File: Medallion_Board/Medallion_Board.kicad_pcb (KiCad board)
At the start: 2 copper layers, 42 parts, among them Q3 DMG3415U, SW1 KMR2, SW2 KMR2, U2 AP2112/RT9080-3.3, U3 ESP32-S3-MINI-1-N8, U4 LC709203FQH-01TWG, U5 MCP73831T-2ACI_OT, X1 JSTPH, X2 USB4085-GF-A

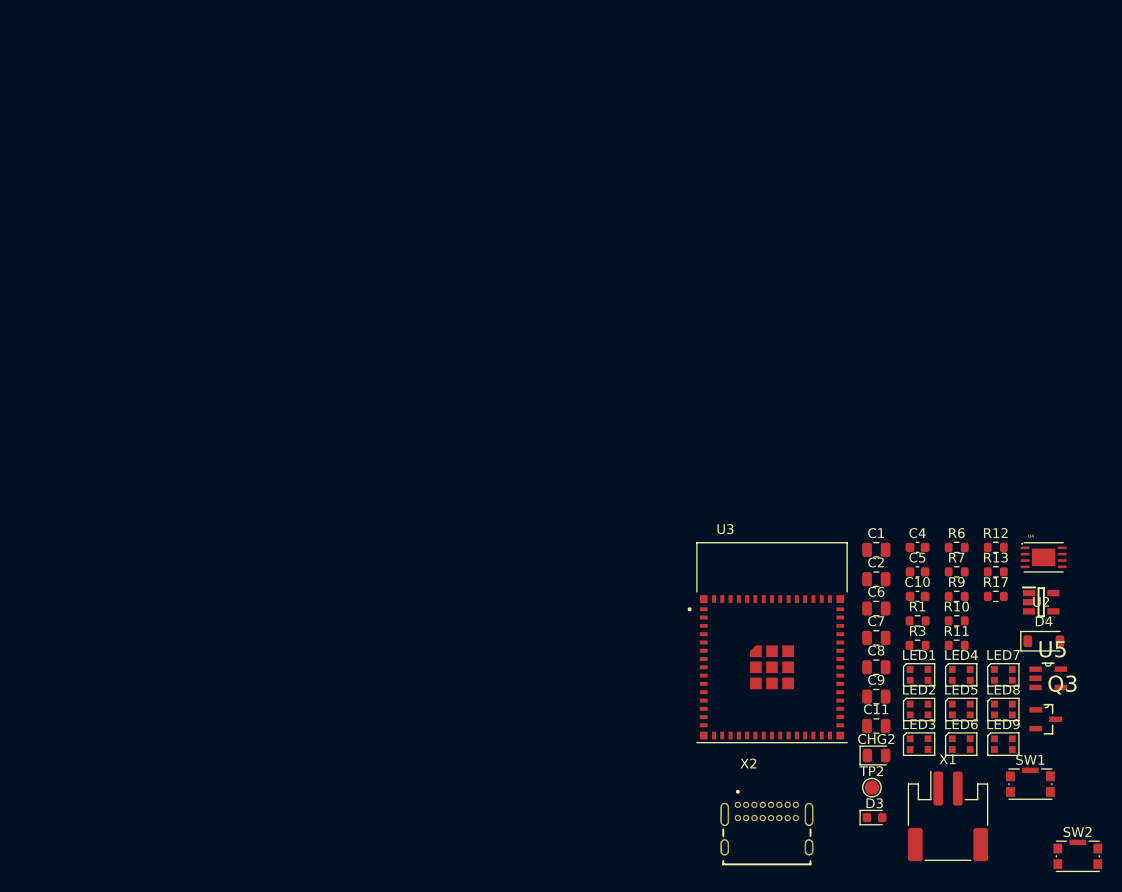
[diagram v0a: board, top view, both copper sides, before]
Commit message: More fiddling. Added 3D models to the components
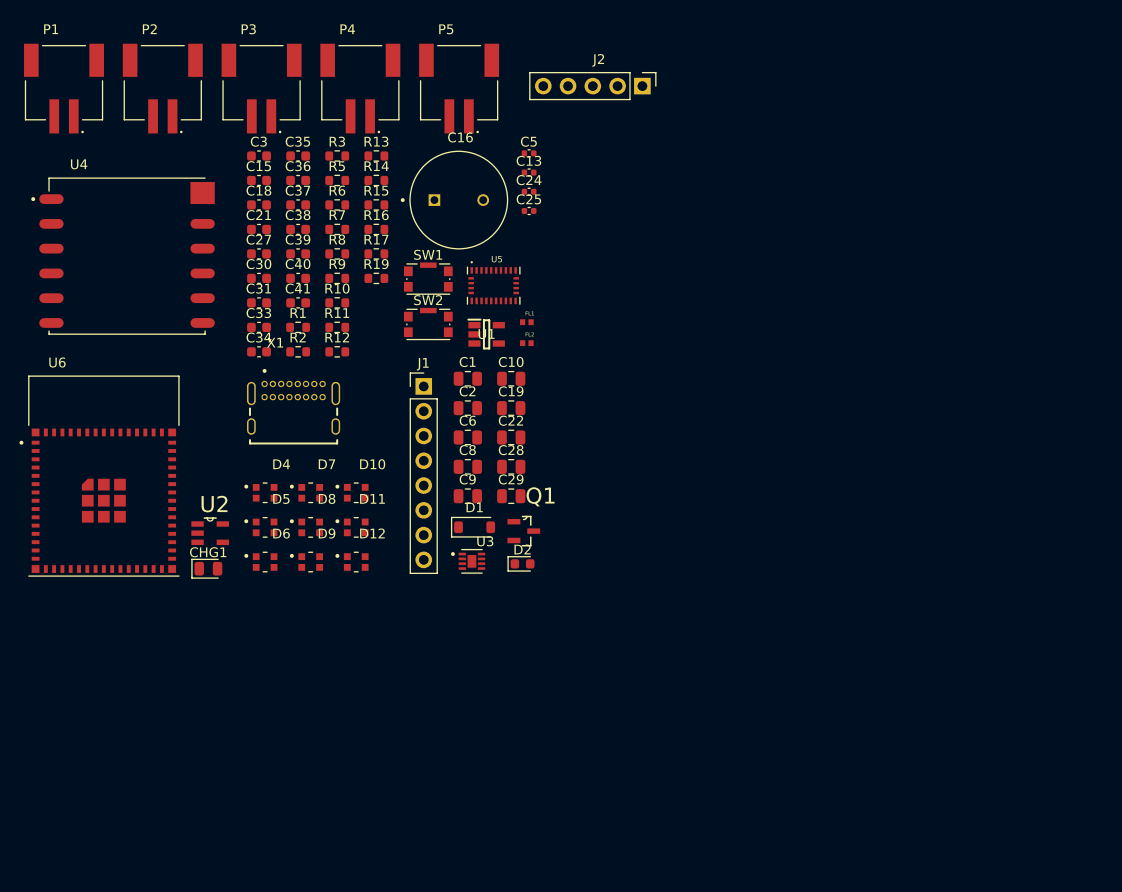
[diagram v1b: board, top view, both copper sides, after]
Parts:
- removed C11: 10µF, Capacitor_SMD:C_0805_2012Metric
- removed C4: 1uF, Capacitor_SMD:C_0603_1608Metric
- removed C7: 10uF, Capacitor_SMD:C_0805_2012Metric
- removed CHG2: ORANGE, LED_SMD:LED_0805_2012Metric
- removed D3: RED, LED_SMD:LED_0603_1608Metric
- removed LED1, LED2, LED3, LED4, LED5, LED6, LED7, LED8, LED9: WS2812B_SK6805_1515, LED_SMD:LED_WS2812B-2020_PLCC4_2.0x2.0mm
- removed Q3: DMG3415U, DMG3415U-7:SOT95P240X105-3N
- removed TP2: TESTPOINTROUND1.5MMNO, TestPoint:TestPoint_Pad_D1.5mm
- removed X2: USB4085-GF-A, USB4085-GF-A:GCT_USB4085-GF-A_REVB
- added C13: 0.1uF, Capacitor_SMD:C_0402_1005Metric, F.Cu at (71.2, 33.3)
- added C15: 100nF, Capacitor_SMD:C_0603_1608Metric, F.Cu at (43.6, 34.1)
- added C16: KW-5R5C104-R, KW-5R5C104-R:CAPPRD500W60D1000H3150, F.Cu at (64.0, 36.1)
- added C18: 100nF, Capacitor_SMD:C_0603_1608Metric, F.Cu at (43.6, 36.6)
- added C19: 10uF, Capacitor_SMD:C_0805_2012Metric, F.Cu at (69.4, 57.5)
- added C21: 100nF, Capacitor_SMD:C_0603_1608Metric, F.Cu at (43.6, 39.2)
- added C22: 10uF, Capacitor_SMD:C_0805_2012Metric, F.Cu at (69.4, 60.5)
- added C24: 0.1uF, Capacitor_SMD:C_0402_1005Metric, F.Cu at (71.2, 35.3)
- added C25: 47pF, Capacitor_SMD:C_0402_1005Metric, F.Cu at (71.2, 37.3)
- added C27: 100nF, Capacitor_SMD:C_0603_1608Metric, F.Cu at (43.6, 41.7)
- added C28: 10uF, Capacitor_SMD:C_0805_2012Metric, F.Cu at (69.4, 63.5)
- added C29: 10uF, Capacitor_SMD:C_0805_2012Metric, F.Cu at (69.4, 66.5)
- added C3: 1uF, Capacitor_SMD:C_0603_1608Metric, F.Cu at (43.6, 31.6)
- added C30: 1uF, Capacitor_SMD:C_0603_1608Metric, F.Cu at (43.6, 44.2)
- added C31: 1uF, Capacitor_SMD:C_0603_1608Metric, F.Cu at (43.6, 46.7)
- added C33: 0.1µF, Capacitor_SMD:C_0603_1608Metric, F.Cu at (43.6, 49.2)
- added C34: 0.1µF, Capacitor_SMD:C_0603_1608Metric, F.Cu at (43.6, 51.7)
- added C35: 0.1µF, Capacitor_SMD:C_0603_1608Metric, F.Cu at (47.6, 31.6)
- added C36: 0.1µF, Capacitor_SMD:C_0603_1608Metric, F.Cu at (47.6, 34.1)
- added C37: 0.1µF, Capacitor_SMD:C_0603_1608Metric, F.Cu at (47.6, 36.6)
- added C38: 0.1µF, Capacitor_SMD:C_0603_1608Metric, F.Cu at (47.6, 39.2)
- added C39: 0.1µF, Capacitor_SMD:C_0603_1608Metric, F.Cu at (47.6, 41.7)
- added C40: 0.1µF, Capacitor_SMD:C_0603_1608Metric, F.Cu at (47.6, 44.2)
- added C41: 0.1µF, Capacitor_SMD:C_0603_1608Metric, F.Cu at (47.6, 46.7)
- added CHG1: ORANGE, LED_SMD:LED_0805_2012Metric, F.Cu at (38.4, 73.9)
- added D1: MBR0540, Diode_SMD:D_SOD-123, F.Cu at (65.7, 69.7)
- added D10: WS2812B2020, WS2812B2020:LED_WS2812B2020, F.Cu at (53.5, 66.2)
- added D11: WS2812B2020, WS2812B2020:LED_WS2812B2020, F.Cu at (53.5, 69.7)
- added D12: WS2812B2020, WS2812B2020:LED_WS2812B2020, F.Cu at (53.5, 73.3)
- added D2: RED, LED_SMD:LED_0603_1608Metric, F.Cu at (70.6, 73.4)
- added D5: WS2812B2020, WS2812B2020:LED_WS2812B2020, F.Cu at (44.2, 69.7)
- added D6: WS2812B2020, WS2812B2020:LED_WS2812B2020, F.Cu at (44.2, 73.3)
- added D7: WS2812B2020, WS2812B2020:LED_WS2812B2020, F.Cu at (48.9, 66.2)
- added D8: WS2812B2020, WS2812B2020:LED_WS2812B2020, F.Cu at (48.9, 69.7)
- added D9: WS2812B2020, WS2812B2020:LED_WS2812B2020, F.Cu at (48.9, 73.3)
- added FL1: BLM15EG121SN1D, BLM15EG121SN1D:BEADC1005X55N, F.Cu at (71.0, 48.7)
- added FL2: BLM15EG121SN1D, BLM15EG121SN1D:BEADC1005X55N, F.Cu at (71.0, 50.8)
- added J1: EXPANSION, Connector_PinHeader_2.54mm:PinHeader_1x08_P2.54mm_Vertical, F.Cu at (60.4, 55.3)
- added J2: RYLR998, Connector_PinHeader_2.54mm:RYLR998, F.Cu at (77.9, 24.2)
- added P1: JST_EN, S2B-PH-SM4-TB_LF__SN_:JST_S2B-PH-SM4-TB_LF__SN_, F.Cu at (23.6, 27.6)
- added P2: JST_PH, S2B-PH-SM4-TB_LF__SN_:JST_S2B-PH-SM4-TB_LF__SN_, F.Cu at (33.7, 27.6)
- added P3: JST_BTN_1, S2B-PH-SM4-TB_LF__SN_:JST_S2B-PH-SM4-TB_LF__SN_, F.Cu at (43.8, 27.6)
- added P4: JST_BTN_2, S2B-PH-SM4-TB_LF__SN_:JST_S2B-PH-SM4-TB_LF__SN_, F.Cu at (53.9, 27.6)
- added P5: JST_BTN_3, S2B-PH-SM4-TB_LF__SN_:JST_S2B-PH-SM4-TB_LF__SN_, F.Cu at (64.1, 27.6)
- added Q1: DMG3415U, DMG3415U-7:SOT95P240X105-3N, F.Cu at (70.7, 70.1)
- added R14: 10K, Resistor_SMD:R_0603_1608Metric, F.Cu at (55.6, 34.1)
- added R15: 10K, Resistor_SMD:R_0603_1608Metric, F.Cu at (55.6, 36.6)
- added R16: 5.1K, Resistor_SMD:R_0603_1608Metric, F.Cu at (55.6, 39.2)
- added R19: 0.5K, Resistor_SMD:R_0603_1608Metric, F.Cu at (55.6, 44.2)
- added R2: 5.1K, Resistor_SMD:R_0603_1608Metric, F.Cu at (47.6, 51.7)
- added R5: 100K, Resistor_SMD:R_0603_1608Metric, F.Cu at (51.6, 34.1)
- added R8: 5.1K, Resistor_SMD:R_0603_1608Metric, F.Cu at (51.6, 41.7)
- added U1: RT9080-33GJ5, RT9080-33GJ5:SOT94P280X100-5N, F.Cu at (66.9, 49.9)
- added U6: ESP32-S3-MINI-1-N8, ESP32-S3-MINI-1-N8:XCVR_ESP32-S3-MINI-1-N8, F.Cu at (27.6, 67.0)
- C1: value 10uF -> 22µF
- C10: value 1uF -> 10uF; footprint Capacitor_SMD:C_0603_1608Metric -> Capacitor_SMD:C_0805_2012Metric
- C2: value 10uF -> 10µF
- C5: value 1uF -> 0.1µF; footprint Capacitor_SMD:C_0603_1608Metric -> Capacitor_SMD:C_0402_1005Metric
- D4: value MBR540 -> WS2812B2020; footprint Diode_SMD:D_SOD-123 -> WS2812B2020:LED_WS2812B2020
- R1: value 5.1K -> 100K
- R10, R11, R13, R9: value 5.1K -> 10K
- R12: value 100K -> 1K
- R3: value 10K -> 2K
- R7: value 100K -> 5.1K
- U2: value AP2112/RT9080-3.3 -> MCP73831T-2ACI_OT; footprint RT9080-33GJ5:SOT94P280X100-5N -> MCP73831T-2ACI_OT:SOT95P280X145-5N
- U3: value ESP32-S3-MINI-1-N8 -> MAX17048G_T10; footprint ESP32-S3-MINI-1-N8:XCVR_ESP32-S3-MINI-1-N8 -> MAX17048G_T10:SON50P200X200X80-9N
- U4: value LC709203FQH-01TWG -> LC86LICMD; footprint LC709203FQH-01TWG:DFN300X400X80-8N -> LC86LICMD:MODULE_LC86LICMD
- U5: value MCP73831T-2ACI_OT -> BNO085; footprint MCP73831T-2ACI_OT:SOT95P280X145-5N -> BNO085:IC_BNO085
- X1: value JSTPH -> USB4085-GF-A; footprint Connector_JST:JST_PH_S2B-PH-SM4-TB_1x02-1MP_P2.00mm_Horizontal -> USB4085-GF-A:GCT_USB4085-GF-A_REVB
- moved U4 98.9 mm to (30.0, 41.9)
- moved SW2 86.1 mm to (60.9, 48.9)
- moved U2 85.5 mm to (38.6, 70.3)
- moved D4 81.3 mm to (44.2, 66.2)
- moved SW1 80.6 mm to (60.9, 44.2)
- moved X1 78.1 mm to (47.1, 59.4)
- moved R3 77.8 mm to (51.6, 31.6)
- moved R13 76.5 mm to (55.6, 31.6)
- moved R17 72.6 mm to (55.6, 41.7)
- moved R7 72.6 mm to (51.6, 39.2)
- moved R6 72.6 mm to (51.6, 36.6)
- moved R11 71.4 mm to (51.6, 49.2)
- moved R9 71.4 mm to (51.6, 44.2)
- moved R10 71.4 mm to (51.6, 46.7)
- moved R12 70.4 mm to (51.6, 51.7)
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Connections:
- C1 pad 1: 3.3V -> VBAT
- C2 pad 1: 3.3V -> /VHI
- C5 pad 1: /IO34_DBLTAP -> Net-(U1-P4)
- C6 pad 1: /VHI -> 3.3V
- C8 pad 1: 3.3V -> VBAT
- D4 pad 1: VBUS -> Net-(D4-DO)
- D4 pad 2: /VHI -> GND
- R1 pad 1: /RESET -> GND
- R1 pad 2: 3.3V -> VBUS
- R10 pad 1: /D13 -> /SDA
- R10 pad 2: Net-(D3-Pad2) -> +3.3V
- R11 pad 1: GND -> /USER_BTN_1
- R11 pad 2: Net-(X2-CC1) -> +3.3V
- R12 pad 1: GND -> 3.3V
- R12 pad 2: VBUS -> Net-(U4-V_BCKP)
- R13 pad 1: GND -> /USER_BTN_2
- R13 pad 2: Net-(X2-CC2) -> +3.3V
- R3 pad 1: /SCL -> GND
- R3 pad 2: /SDA -> Net-(U2-PROG)
- R6 pad 2: Net-(U5-STAT) -> Net-(U2-STAT)
- R7 pad 1: /EN -> GND
- R7 pad 2: /VHI -> Net-(X1-CC1)
- R9 pad 1: GND -> /SCL
- R9 pad 2: Net-(U5-PROG) -> +3.3V
- SW1 pad 2: /BOOT0 -> /RESET
- SW2 pad 2: /RESET -> /BOOT0
- U2 pad 1: /VHI -> Net-(U2-STAT)
- U2 pad 3: /EN -> VBAT
- U2 pad 4: unconnected-(U2-P4-Pad4) -> VBUS
- U2 pad 5: 3.3V -> Net-(U2-PROG)
- U3 pad 2: GND -> VBAT
- U3 pad 3: 3.3V -> VBAT
- U3 pad 4: /BOOT0 -> GND
- U3 pad 5: unconnected-(U3-IO1-Pad5) -> /LOW_BATT
- U3 pad 6: unconnected-(U3-IO2-Pad6) -> GND
- U3 pad 7: /SDA -> /SCL
- U3 pad 8: /SCL -> /SDA
- U3 pad 9: unconnected-(U3-IO5-Pad9) -> GND
- U4 pad 1: GND -> /TXD0
- U4 pad 2: GND -> /RXD0
- U4 pad 3: VBAT -> GND
- U4 pad 4: unconnected-(U4-ALARMB-Pad4) -> 3.3V
- U4 pad 5: unconnected-(U4-TSW-Pad5) -> Net-(U4-V_BCKP)
- U4 pad 7: /SDA -> /GPS_WAKEUP
- U4 pad 8: /SCL -> /GPS_ANT_ACTIVE
- U5 pad 1: Net-(U5-STAT) -> unconnected-(U5-RESV_NC-Pad1)
- U5 pad 3: VBAT -> 3.3V
- U5 pad 4: VBUS -> Net-(U5-~{BOOT})
- U5 pad 5: Net-(U5-PROG) -> GND

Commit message: Categorise pcb layout by specsheet boxes
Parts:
- removed C33, C34, C35, C36, C37, C38, C39, C40, C41: 0.1µF, Capacitor_SMD:C_0603_1608Metric
- removed D12: WS2812B2020, WS2812B2020:LED_WS2812B2020
- removed R19: 0.5K, Resistor_SMD:R_0603_1608Metric
- added C11: 10uF, Capacitor_SMD:C_0805_2012Metric, F.Cu at (86.2, 78.0)
- added C12: 0.1µF, Capacitor_SMD:C_0402_1005Metric, F.Cu at (96.7, 88.0)
- added C14: 1uF, Capacitor_SMD:C_0603_1608Metric, F.Cu at (238.5, 145.5)
- added C17: 100nF, Capacitor_SMD:C_0603_1608Metric, F.Cu at (202.4, 86.4)
- added C20: 100nF, Capacitor_SMD:C_0603_1608Metric, F.Cu at (119.2, 175.0)
- added C23: 0.1µF, Capacitor_SMD:C_0603_1608Metric, F.Cu at (26.5, 25.9)
- added C26: 0.1µF, Capacitor_SMD:C_0603_1608Metric, F.Cu at (41.0, 32.8)
- added C4: KW-5R5C104-R, KW-5R5C104-R:CAPPRD500W60D1000H3150, F.Cu at (150.5, 28.5)
- added C7: 0.1uF, Capacitor_SMD:C_0402_1005Metric, F.Cu at (45.0, 143.5)
- added D3: WS2812B2020, WS2812B2020:LED_WS2812B2020, F.Cu at (25.4, 32.5)
- added R4: 1Meg, Resistor_SMD:R_0603_1608Metric, F.Cu at (246.5, 145.5)
- C1: value 22µF -> 10uF
- C10, C9: value 10uF -> 10µF
- C13: value 0.1uF -> 10uF; footprint Capacitor_SMD:C_0402_1005Metric -> Capacitor_SMD:C_0805_2012Metric
- C16: value KW-5R5C104-R -> 100nF; footprint KW-5R5C104-R:CAPPRD500W60D1000H3150 -> Capacitor_SMD:C_0603_1608Metric
- C18: value 100nF -> 1uF
- C19: value 10uF -> 0.1uF; footprint Capacitor_SMD:C_0805_2012Metric -> Capacitor_SMD:C_0402_1005Metric
- C2, C6: value 10µF -> 10uF
- C21: value 100nF -> 10µF; footprint Capacitor_SMD:C_0603_1608Metric -> Capacitor_SMD:C_0805_2012Metric
- C22, C28, C29: value 10uF -> 0.1µF; footprint Capacitor_SMD:C_0805_2012Metric -> Capacitor_SMD:C_0603_1608Metric
- C24: value 0.1uF -> 0.1µF; footprint Capacitor_SMD:C_0402_1005Metric -> Capacitor_SMD:C_0603_1608Metric
- C25: value 47pF -> 0.1µF; footprint Capacitor_SMD:C_0402_1005Metric -> Capacitor_SMD:C_0603_1608Metric
- C27: value 100nF -> 0.1µF
- C30: value 1uF -> 0.1µF
- C31: value 1uF -> 22µF; footprint Capacitor_SMD:C_0603_1608Metric -> Capacitor_SMD:C_0805_2012Metric
- C5: value 0.1µF -> 10uF; footprint Capacitor_SMD:C_0402_1005Metric -> Capacitor_SMD:C_0805_2012Metric
- C8: value 10µF -> 47pF; footprint Capacitor_SMD:C_0805_2012Metric -> Capacitor_SMD:C_0402_1005Metric
- J1: value EXPANSION -> RYLR998; footprint Connector_PinHeader_2.54mm:PinHeader_1x08_P2.54mm_Vertical -> Connector_PinHeader_2.54mm:RYLR998
- J2: value RYLR998 -> EXPANSION; footprint Connector_PinHeader_2.54mm:RYLR998 -> Connector_PinHeader_2.54mm:PinHeader_1x08_P2.54mm_Vertical
- P1: value JST_EN -> JST_PH
- P2: value JST_PH -> JST_BTN_1
- P3: value JST_BTN_1 -> JST_BTN_2
- P4: value JST_BTN_2 -> JST_BTN_3
- P5: value JST_BTN_3 -> JST_EN
- R1: value 100K -> 1K
- R12: value 1K -> 10K
- R14: value 10K -> 5.1K
- R15: value 10K -> 2K
- R17: value 1Meg -> 0.5K
- R2: value 5.1K -> 100K
- R3: value 2K -> 100K
- R5: value 100K -> 5.1K
- R8: value 5.1K -> 10K
- U2: value MCP73831T-2ACI_OT -> LC86LICMD; footprint MCP73831T-2ACI_OT:SOT95P280X145-5N -> LC86LICMD:MODULE_LC86LICMD
- U3: value MAX17048G_T10 -> ESP32-S3-MINI-1-N8; footprint MAX17048G_T10:SON50P200X200X80-9N -> ESP32-S3-MINI-1-N8:XCVR_ESP32-S3-MINI-1-N8
- U4: value LC86LICMD -> BNO085; footprint LC86LICMD:MODULE_LC86LICMD -> BNO085:IC_BNO085
- U5: value BNO085 -> MAX17048G_T10; footprint BNO085:IC_BNO085 -> MAX17048G_T10:SON50P200X200X80-9N
- U6: value ESP32-S3-MINI-1-N8 -> MCP73831T-2ACI_OT; footprint ESP32-S3-MINI-1-N8:XCVR_ESP32-S3-MINI-1-N8 -> MCP73831T-2ACI_OT:SOT95P280X145-5N
- moved C3 224.5 mm to (238.5, 143.0)
- moved X1 215.9 mm to (263.0, 54.5)
- moved C18 210.7 mm to (254.0, 48.1)
- moved R5 210.5 mm to (262.0, 40.6)
- moved R6 210.5 mm to (262.0, 43.1)
- moved R7 210.5 mm to (262.0, 45.6)
- moved SW1 208.1 mm to (268.9, 38.6)
- moved SW2 208.1 mm to (268.9, 43.3)
- moved C1 198.4 mm to (242.5, 143.0)
- moved C2 198.4 mm to (242.5, 146.0)
- moved R11 195.2 mm to (227.3, 134.1)
- moved U3 192.8 mm to (249.0, 132.0)
- moved R12 192.1 mm to (227.7, 128.5)
- moved P5 189.7 mm to (253.2, 43.2)
- moved J2 168.3 mm to (214.0, 123.3), turned to 0 degrees
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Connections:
- C1 pad 1: VBAT -> 3.3V
- C13 pad 1: GND -> 3.3V
- C13 pad 2: VBAT -> GND
- C16 pad 1: Net-(U4-V_BCKP) -> GND
- C16 pad 2: GND -> /USER_BTN_2
- C18 pad 1: GND -> /RESET
- C18 pad 2: /USER_BTN_2 -> GND
- C19 pad 1: +3.3V -> GND
- C19 pad 2: GND -> VBAT
- C2 pad 1: /VHI -> 3.3V
- C21 pad 1: GND -> VBAT
- C21 pad 2: /USER_BTN_3 -> GND
- C22 pad 1: Net-(J2-VDD) -> VBAT
- C24 pad 1: Net-(J2-VDD) -> VBAT
- C25 pad 1: Net-(J2-VDD) -> VBAT
- C27 pad 1: Net-(U5-CAP) -> VBAT
- C28 pad 1: 3.3V -> VBAT
- C29 pad 1: 3.3V -> VBAT
- C3 pad 1: /RESET -> 3.3V
- C30 pad 1: 3.3V -> VBAT
- C31 pad 1: /IO34_DBLTAP -> VBAT
- C5 pad 1: Net-(U1-P4) -> +3.3V
- C6 pad 1: 3.3V -> Net-(J1-VDD)
- C8 pad 1: VBAT -> Net-(J1-VDD)
- C9 pad 1: 3.3V -> /VHI
- D11 pad 1: Net-(D11-DO) -> unconnected-(D11-DO-Pad1)
- FL1 pad 2: Net-(J2-VDD) -> Net-(J1-VDD)
- J1 pad 1: /GPIO01 -> Net-(J1-VDD)
- J1 pad 2: /GPIO02 -> /LORA_NRST
- J1 pad 3: /GPIO06 -> /TXD1
- J1 pad 4: /GPIO11 -> /RXD1
- J1 pad 5: /SDA -> GND
- J2 pad 1: Net-(J2-VDD) -> /GPIO01
- J2 pad 2: /LORA_NRST -> /GPIO02
- J2 pad 3: /TXD1 -> /GPIO06
- J2 pad 4: /RXD1 -> /GPIO11
- J2 pad 5: GND -> /SDA
- P1 pad 1: /RESET -> VBAT
- P2 pad 1: VBAT -> /USER_BTN_1
- P3 pad 1: /USER_BTN_1 -> /USER_BTN_2
- P4 pad 1: /USER_BTN_2 -> /USER_BTN_3
- P5 pad 1: /USER_BTN_3 -> /RESET
- R1 pad 1: GND -> 3.3V
- R1 pad 2: VBUS -> Net-(U2-V_BCKP)
- R10 pad 1: /SDA -> /USER_BTN_3
- R11 pad 1: /USER_BTN_1 -> /SCL
- R12 pad 1: 3.3V -> /SDA
- R12 pad 2: Net-(U4-V_BCKP) -> +3.3V
- R13 pad 1: /USER_BTN_2 -> Net-(U4-~{BOOT})
- R13 pad 2: +3.3V -> 3.3V
- R14 pad 1: Net-(U5-~{BOOT}) -> Net-(CHG1-Pad1)
- R14 pad 2: 3.3V -> Net-(U6-STAT)
- R15 pad 1: /USER_BTN_3 -> GND
- R15 pad 2: +3.3V -> Net-(U6-PROG)
- R17 pad 1: GND -> Net-(D3-DI)
- R17 pad 2: /IO34_DBLTAP -> /NEOPIX
- R2 pad 1: /RESET -> Net-(U1-EN)
- R2 pad 2: 3.3V -> /VHI
- R3 pad 2: Net-(U2-PROG) -> VBUS
- R5 pad 1: Net-(U1-EN) -> GND
- R5 pad 2: /VHI -> Net-(X1-CC1)
- R6 pad 1: Net-(CHG1-Pad1) -> GND
- R6 pad 2: Net-(U2-STAT) -> Net-(X1-CC2)
- R7 pad 1: GND -> /RESET
- R7 pad 2: Net-(X1-CC1) -> 3.3V
- R8 pad 1: GND -> /USER_BTN_1
- R8 pad 2: Net-(X1-CC2) -> +3.3V
- R9 pad 1: /SCL -> /USER_BTN_2
- U2 pad 1: Net-(U2-STAT) -> /TXD0
- U2 pad 2: GND -> /RXD0
- U2 pad 3: VBAT -> GND
- U2 pad 4: VBUS -> 3.3V
- U2 pad 5: Net-(U2-PROG) -> Net-(U2-V_BCKP)
- U3 pad 2: VBAT -> GND
- U3 pad 3: VBAT -> 3.3V
- U3 pad 4: GND -> /BOOT0
- U3 pad 5: /LOW_BATT -> /GPIO01
- U3 pad 6: GND -> /GPIO02
- U3 pad 7: /SCL -> /SDA
- U3 pad 8: /SDA -> /SCL
- U3 pad 9: GND -> /LOW_BATT
- U4 pad 1: /TXD0 -> unconnected-(U4-RESV_NC-Pad1)
- U4 pad 10: /GPS_RESET -> unconnected-(U4-CLKSEL0-Pad10)
- U4 pad 11: unconnected-(U4-EX_ANT-Pad11) -> /BNO_NRST
- U4 pad 12: GND -> unconnected-(U4-RESV_NC-Pad12)
- U4 pad 2: /RXD0 -> GND
- U4 pad 3: GND -> 3.3V
- U4 pad 4: 3.3V -> Net-(U4-~{BOOT})
- U4 pad 5: Net-(U4-V_BCKP) -> GND
- U4 pad 6: unconnected-(U4-1PPS-Pad6) -> GND
- U4 pad 7: /GPS_WAKEUP -> unconnected-(U4-RESV_NC-Pad7)
- U4 pad 8: /GPS_ANT_ACTIVE -> unconnected-(U4-RESV_NC-Pad8)
- U4 pad 9: unconnected-(U4-RESERVED-Pad9) -> Net-(U4-CAP)
- U5 pad 1: unconnected-(U5-RESV_NC-Pad1) -> GND
- U5 pad 2: GND -> VBAT
- U5 pad 3: 3.3V -> VBAT
- U5 pad 4: Net-(U5-~{BOOT}) -> GND
- U5 pad 5: GND -> /LOW_BATT
- U5 pad 7: unconnected-(U5-RESV_NC-Pad7) -> /SCL
- U5 pad 8: unconnected-(U5-RESV_NC-Pad8) -> /SDA
- U5 pad 9: Net-(U5-CAP) -> GND
- U6 pad 1: GND -> Net-(U6-STAT)
- U6 pad 3: 3.3V -> VBAT
- U6 pad 4: /BOOT0 -> VBUS
- U6 pad 5: /GPIO01 -> Net-(U6-PROG)

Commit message: Migrate to the nRF microcontroller. Attempt to implement my own lora section - will probably remove later.
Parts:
- removed FL1, FL2: BLM15EG121SN1D, BLM15EG121SN1D:BEADC1005X55N
- added IC1: 114993121, Wio-E5-LE:114993121, F.Cu at (136.0, 177.8)
- added L1: 10uH, LQM18DN100M70L:INDC1608X95N, F.Cu at (42.9, 52.2)
- added L2: 0R, LQM18DN100M70L:INDC1608X95N, F.Cu at (147.5, 186.8)
- added R18: 5.1K, Resistor_SMD:R_0603_1608Metric, F.Cu at (77.7, 175.0)
- added R19: 5.1K, Resistor_SMD:R_0603_1608Metric, F.Cu at (82.7, 175.0)
- added R20: 27R, Resistor_SMD:R_0603_1608Metric, F.Cu at (79.7, 171.0)
- added R21: 10K, Resistor_SMD:R_0603_1608Metric, F.Cu at (25.1, 181.7)
- added R22: 27R, Resistor_SMD:R_0603_1608Metric, F.Cu at (84.2, 171.0)
- added R23: 5.6K, Resistor_SMD:R_0603_1608Metric, F.Cu at (132.0, 193.0)
- added R24: 22R, Resistor_SMD:R_0603_1608Metric, F.Cu at (132.0, 188.5)
- added R25: 22R, Resistor_SMD:R_0603_1608Metric, F.Cu at (135.2, 190.5)
- added Y1: 32.768KHZ, ABS07-32.768KHZ-7-T:XTAL_ABS07-32.768KHZ-7-T, F.Cu at (68.2, 39.9)
- C1, C2: value 10uF -> 12pF; footprint Capacitor_SMD:C_0805_2012Metric -> Capacitor_SMD:C_0402_1005Metric
- C10: value 10µF -> 0.1µF; footprint Capacitor_SMD:C_0805_2012Metric -> Capacitor_SMD:C_0402_1005Metric
- C11, C13: value 10uF -> 10µF
- C12: value 0.1µF -> 10uF; footprint Capacitor_SMD:C_0402_1005Metric -> Capacitor_SMD:C_0805_2012Metric
- C14, C3: value 1uF -> 10uF; footprint Capacitor_SMD:C_0603_1608Metric -> Capacitor_SMD:C_0805_2012Metric
- C15, C16, C17, C20: value 100nF -> 0.1µF
- C18: value 1uF -> 0.1µF
- C19: value 0.1uF -> 0.1µF; footprint Capacitor_SMD:C_0402_1005Metric -> Capacitor_SMD:C_0603_1608Metric
- C21: value 10µF -> 0.1µF; footprint Capacitor_SMD:C_0805_2012Metric -> Capacitor_SMD:C_0603_1608Metric
- C24, C25, C27, C29: value 0.1µF -> 100nF
- C26: value 0.1µF -> 22µF; footprint Capacitor_SMD:C_0603_1608Metric -> Capacitor_SMD:C_0805_2012Metric
- C28: value 0.1µF -> 4.7uF
- C30: value 0.1µF -> NC
- C31: value 22µF -> NC; footprint Capacitor_SMD:C_0805_2012Metric -> Capacitor_SMD:C_0603_1608Metric
- C4: value KW-5R5C104-R -> 10uF; footprint KW-5R5C104-R:CAPPRD500W60D1000H3150 -> Capacitor_SMD:C_0805_2012Metric
- C6: value 10uF -> 1uF; footprint Capacitor_SMD:C_0805_2012Metric -> Capacitor_SMD:C_0603_1608Metric
- C8: value 47pF -> 100mF; footprint Capacitor_SMD:C_0402_1005Metric -> KW-5R5C104-R:CAPPRD500W60D1000H3150
- J1: value RYLR998 -> EXPANSION; footprint Connector_PinHeader_2.54mm:RYLR998 -> Connector_PinHeader_2.54mm:PinHeader_1x08_P2.54mm_Vertical
- J2: value EXPANSION -> RECE.20369.001E.01; footprint Connector_PinHeader_2.54mm:PinHeader_1x08_P2.54mm_Vertical -> RECE.20369:RECE20369001E01
- P1: value JST_PH -> JST_ONOFF
- P2: value JST_BTN_1 -> JST_PH
- P3: value JST_BTN_2 -> JST_BTN_1
- P5: value JST_EN -> JST_BTN_2
- R1: value 1K -> 5.1K
- R10, R11: value 10K -> 1K
- R15: value 2K -> 0.5K
- R16: value 5.1K -> 10K
- R17: value 0.5K -> 470R
- R2, R3: value 100K -> 10K
- R4: value 1Meg -> 100K
- R5: value 5.1K -> 1K
- R7: value 5.1K -> 5.6K
- R8: value 10K -> 2K
- R9: value 10K -> 100K
- U1: value RT9080-33GJ5 -> MDBT50Q-1MV2; footprint RT9080-33GJ5:SOT94P280X100-5N -> MDBT50Q-1MV2:XCVR_MDBT50Q-1MV2
- U2: value LC86LICMD -> MAX17048G_T10; footprint LC86LICMD:MODULE_LC86LICMD -> MAX17048G_T10:SON50P200X200X80-9N
- U3: value ESP32-S3-MINI-1-N8 -> LC86LICMD; footprint ESP32-S3-MINI-1-N8:XCVR_ESP32-S3-MINI-1-N8 -> LC86LICMD:MODULE_LC86LICMD
- U4: value BNO085 -> RT9080-33GJ5; footprint BNO085:IC_BNO085 -> RT9080-33GJ5:SOT94P280X100-5N
- U5: value MAX17048G_T10 -> MCP73831T-2ACI_OT; footprint MAX17048G_T10:SON50P200X200X80-9N -> MCP73831T-2ACI_OT:SOT95P280X145-5N
- U6: value MCP73831T-2ACI_OT -> BNO085; footprint MCP73831T-2ACI_OT:SOT95P280X145-5N -> BNO085:IC_BNO085
- moved C23 255.6 mm to (257.8, 134.5), turned to 180 degrees
- moved C22 249.0 mm to (249.3, 134.5), turned to 180 degrees
- moved D11 240.7 mm to (257.6, 130.5)
- moved D10 234.3 mm to (249.2, 130.5)
- moved D9 228.2 mm to (240.8, 130.5)
- moved R6 226.0 mm to (42.2, 95.6), turned to 90 degrees
- moved X1 223.7 mm to (80.6, 184.0)
- moved D8 221.8 mm to (232.4, 130.5)
- moved D7 215.7 mm to (224.0, 130.5)
- moved D6 209.8 mm to (215.6, 130.5)
- moved SW1 209.5 mm to (59.9, 24.4)
- moved C3 206.1 mm to (53.4, 52.5), turned to -90 degrees
- moved C2 204.2 mm to (65.9, 43.4), turned to -90 degrees
- moved D5 203.3 mm to (207.2, 130.5)
- moved C1 199.3 mm to (69.9, 43.4), turned to -90 degrees
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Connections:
- C1 pad 1: 3.3V -> GND
- C1 pad 2: GND -> /OSC1
- C10 pad 1: 3.3V -> Net-(U4-P4)
- C12 pad 1: Net-(U1-P4) -> 3.3V
- C13 pad 1: 3.3V -> VBAT
- C14 pad 1: /IO34_DBLTAP -> 3.3V
- C15 pad 1: GND -> VBAT
- C15 pad 2: /USER_BTN_1 -> GND
- C16 pad 1: GND -> VBAT
- C16 pad 2: /USER_BTN_2 -> GND
- C17 pad 1: GND -> VBAT
- C17 pad 2: /USER_BTN_3 -> GND
- C18 pad 1: /RESET -> VBAT
- C19 pad 1: GND -> VBAT
- C19 pad 2: VBAT -> GND
- C2 pad 1: 3.3V -> GND
- C2 pad 2: GND -> /OSC2
- C20 pad 1: Net-(U4-CAP) -> VBAT
- C24 pad 1: VBAT -> GND
- C24 pad 2: GND -> /USER_BTN_1
- C25 pad 1: VBAT -> GND
- C25 pad 2: GND -> /USER_BTN_3
- C27 pad 1: VBAT -> GND
- C27 pad 2: GND -> /USER_BTN_2
- C28 pad 1: VBAT -> 3.3V
- C29 pad 1: VBAT -> Net-(U6-CAP)
- C3 pad 1: 3.3V -> Net-(U1-VDD)
- C30 pad 1: VBAT -> Net-(IC1-RFIO)
- C31 pad 1: VBAT -> GND
- C4 pad 1: Net-(U2-V_BCKP) -> 3.3V
- C5 pad 1: +3.3V -> VBUS
- C6 pad 1: Net-(J1-VDD) -> /uC_RESET
- C7 pad 1: Net-(J1-VDD) -> GND
- C7 pad 2: GND -> VBAT
- C8 pad 1: Net-(J1-VDD) -> Net-(U3-V_BCKP)
- J1 pad 1: Net-(J1-VDD) -> /GPIO19
- J1 pad 2: /LORA_NRST -> /GPIO20
- J1 pad 3: /TXD1 -> /GPIO21
- J1 pad 4: /RXD1 -> /GPIO22
- J1 pad 5: GND -> /SDA
- J2 pad 1: /GPIO01 -> GND
- J2 pad 2: /GPIO02 -> GND
- J2 pad 3: /GPIO06 -> GND
- J2 pad 4: /GPIO11 -> GND
- P1 pad 1: VBAT -> Net-(U4-EN)
- P2 pad 1: /USER_BTN_1 -> VBAT
- P3 pad 1: /USER_BTN_2 -> /USER_BTN_1
- P5 pad 1: /RESET -> /USER_BTN_2
- R1 pad 1: 3.3V -> /uC_RESET
- R1 pad 2: Net-(U2-V_BCKP) -> 3.3V
- R10 pad 1: /USER_BTN_3 -> /TXD_GPS
- R10 pad 2: +3.3V -> Net-(U3-RXD)
- R11 pad 1: /SCL -> Net-(U3-TXD)
- R11 pad 2: +3.3V -> /RXD_GPS
- R12 pad 1: /SDA -> /USER_BTN_1
- R12 pad 2: +3.3V -> 3.3V
- R13 pad 1: Net-(U4-~{BOOT}) -> /USER_BTN_3
- R14 pad 1: Net-(CHG1-Pad1) -> /STATUS_LED
- R14 pad 2: Net-(U6-STAT) -> Net-(D2-Pad2)
- R15 pad 1: GND -> Net-(D3-DI)
- R15 pad 2: Net-(U6-PROG) -> /NEOPIX
- R16 pad 1: /STATUS_LED -> /USER_BTN_2
- R16 pad 2: Net-(D2-Pad2) -> 3.3V
- R17 pad 1: Net-(D3-DI) -> Net-(R17-Pad1)
- R17 pad 2: /NEOPIX -> GND
- R2 pad 1: Net-(U1-EN) -> /SCL
- R2 pad 2: /VHI -> 3.3V
- R3 pad 1: GND -> /SDA
- R3 pad 2: VBUS -> 3.3V
- R4 pad 1: GND -> /VHI
- R4 pad 2: /IO34_DBLTAP -> Net-(U4-EN)
- R5 pad 1: GND -> 3.3V
- R5 pad 2: Net-(X1-CC1) -> Net-(U3-V_BCKP)
- R6 pad 1: GND -> Net-(CHG1-Pad1)
- R6 pad 2: Net-(X1-CC2) -> Net-(U5-STAT)
- R7 pad 1: /RESET -> Net-(U3-RXD)
- R7 pad 2: 3.3V -> GND
- R8 pad 1: /USER_BTN_1 -> GND
- R8 pad 2: +3.3V -> Net-(U5-PROG)
- R9 pad 1: /USER_BTN_2 -> GND
- R9 pad 2: +3.3V -> VBUS
- SW1 pad 2: /RESET -> /uC_RESET
- SW2 pad 1: GND -> Net-(IC1-PB13)
- SW2 pad 2: /BOOT0 -> Net-(R17-Pad1)
- U1 pad 1: /VHI -> GND
- U1 pad 3: Net-(U1-EN) -> /USER_BTN_1
- U1 pad 4: Net-(U1-P4) -> /USER_BTN_2
- U1 pad 5: 3.3V -> /USER_BTN_3
- U2 pad 1: /TXD0 -> GND
- U2 pad 2: /RXD0 -> VBAT
- U2 pad 3: GND -> VBAT
- U2 pad 4: 3.3V -> GND
- U2 pad 5: Net-(U2-V_BCKP) -> /LOW_BATT
- U2 pad 6: unconnected-(U2-1PPS-Pad6) -> GND
- U2 pad 7: /GPS_WAKEUP -> /SCL
- U2 pad 8: /GPS_ANT_ACTIVE -> /SDA
- U2 pad 9: unconnected-(U2-RESERVED-Pad9) -> GND
- U3 pad 1: GND -> Net-(U3-RXD)
- U3 pad 10: /GPIO06 -> /GPS_RESET
- U3 pad 11: /I2C_PWR -> unconnected-(U3-EX_ANT-Pad11)
- U3 pad 12: /GPS_WAKEUP -> GND
- U3 pad 2: GND -> Net-(U3-TXD)
- U3 pad 3: 3.3V -> GND
- U3 pad 4: /BOOT0 -> 3.3V
- U3 pad 5: /GPIO01 -> Net-(U3-V_BCKP)
- U3 pad 6: /GPIO02 -> unconnected-(U3-1PPS-Pad6)
- U3 pad 7: /SDA -> /GPS_WAKEUP
- U3 pad 8: /SCL -> /GPS_ANT_ACTIVE
- U3 pad 9: /LOW_BATT -> unconnected-(U3-RESERVED-Pad9)
- U4 pad 1: unconnected-(U4-RESV_NC-Pad1) -> /VHI
- U4 pad 3: 3.3V -> Net-(U4-EN)
- U4 pad 4: Net-(U4-~{BOOT}) -> Net-(U4-P4)
- U4 pad 5: GND -> 3.3V
- U5 pad 1: GND -> Net-(U5-STAT)
- U5 pad 2: VBAT -> GND
- U5 pad 4: GND -> VBUS
- U5 pad 5: /LOW_BATT -> Net-(U5-PROG)
- U6 pad 1: Net-(U6-STAT) -> unconnected-(U6-RESV_NC-Pad1)
- U6 pad 3: VBAT -> 3.3V
- U6 pad 4: VBUS -> Net-(U6-~{BOOT})
- U6 pad 5: Net-(U6-PROG) -> GND
- X1 pad A6: /D+ -> Net-(X1-DP1)
- X1 pad B6: /D- -> Net-(X1-DP2)
